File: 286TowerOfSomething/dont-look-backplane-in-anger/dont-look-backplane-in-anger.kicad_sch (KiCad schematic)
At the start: 1 part, among them J1 Bus_ISA_16bit

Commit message: More work on dont-look-backplane-in-anger
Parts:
- added J2, J3, J4, J5, J6, J7: Bus_ISA_16bit, pc-parts:645169-3, symbol Connector:Bus_ISA_16bit
- J1: footprint (none) -> pc-parts:645169-3
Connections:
- net GND: now reaches J1.1 (GND)
- net GND: now also J1.10 (GND), J1.31 (GND), J1.80 (GND), J2.1 (GND), J2.10 (GND), J2.31 (GND), J2.80 (GND), J3.1 (GND), J3.10 (GND), J3.31 (GND), J3.80 (GND), J4.1 (GND), J4.10 (GND), J4.31 (GND), J4.80 (GND), J5.1 (GND), J5.10 (GND), J5.31 (GND), J5.80 (GND), J6.1 (GND), J6.10 (GND), J6.31 (GND), J6.80 (GND), J7.1 (GND), J7.10 (GND), J7.31 (GND), J7.80 (GND)
- net ~{MEMWR}: now reaches J1.11 (~{SMEMW})
- net ~{MEMWR}: now also J2.11 (~{SMEMW}), J3.11 (~{SMEMW}), J4.11 (~{SMEMW}), J5.11 (~{SMEMW}), J6.11 (~{SMEMW}), J7.11 (~{SMEMW})
- net ~{MEMRD}: now reaches J1.12 (~{SMEMR})
- net ~{MEMRD}: now also J2.12 (~{SMEMR}), J3.12 (~{SMEMR}), J4.12 (~{SMEMR}), J5.12 (~{SMEMR}), J6.12 (~{SMEMR}), J7.12 (~{SMEMR})
- net ~{IOW}: now reaches J1.13 (~{IOW})
- net ~{IOW}: now also J2.13 (~{IOW}), J3.13 (~{IOW}), J4.13 (~{IOW}), J5.13 (~{IOW}), J6.13 (~{IOW}), J7.13 (~{IOW})
- net ~{IOR}: now reaches J1.14 (~{IOR})
- net ~{IOR}: now also J2.14 (~{IOR}), J3.14 (~{IOR}), J4.14 (~{IOR}), J5.14 (~{IOR}), J6.14 (~{IOR}), J7.14 (~{IOR})
- net ~{DACK3}: now reaches J1.15 (~{DACK3})
- net ~{DACK3}: now also J2.15 (~{DACK3}), J3.15 (~{DACK3}), J4.15 (~{DACK3}), J5.15 (~{DACK3}), J6.15 (~{DACK3}), J7.15 (~{DACK3})
- net DRQ3: now reaches J1.16 (DRQ3)
- net DRQ3: now also J2.16 (DRQ3), J3.16 (DRQ3), J4.16 (DRQ3), J5.16 (DRQ3), J6.16 (DRQ3), J7.16 (DRQ3)
- net ~{DACK1}: now reaches J1.17 (~{DACK1})
- net ~{DACK1}: now also J2.17 (~{DACK1}), J3.17 (~{DACK1}), J4.17 (~{DACK1}), J5.17 (~{DACK1}), J6.17 (~{DACK1}), J7.17 (~{DACK1})
- net DRQ1: now reaches J1.18 (DRQ1)
- net DRQ1: now also J2.18 (DRQ1), J3.18 (DRQ1), J4.18 (DRQ1), J5.18 (DRQ1), J6.18 (DRQ1), J7.18 (DRQ1)
- net ~{REFRESH}: now reaches J1.19 (~{REFRESH})
- net ~{REFRESH}: now also J2.19 (~{REFRESH}), J3.19 (~{REFRESH}), J4.19 (~{REFRESH}), J5.19 (~{REFRESH}), J6.19 (~{REFRESH}), J7.19 (~{REFRESH})
- net RESET: now reaches J1.2 (RESET)
- net RESET: now also J2.2 (RESET), J3.2 (RESET), J4.2 (RESET), J5.2 (RESET), J6.2 (RESET), J7.2 (RESET)
- net CLK: now reaches J1.20 (CLK)
- net CLK: now also J2.20 (CLK), J3.20 (CLK), J4.20 (CLK), J5.20 (CLK), J6.20 (CLK), J7.20 (CLK)
- net IRQ7: now reaches J1.21 (IRQ7)
- net IRQ7: now also J2.21 (IRQ7), J3.21 (IRQ7), J4.21 (IRQ7), J5.21 (IRQ7), J6.21 (IRQ7), J7.21 (IRQ7)
- net IRQ6: now reaches J1.22 (IRQ6)
- net IRQ6: now also J2.22 (IRQ6), J3.22 (IRQ6), J4.22 (IRQ6), J5.22 (IRQ6), J6.22 (IRQ6), J7.22 (IRQ6)
- net IRQ5: now reaches J1.23 (IRQ5)
- net IRQ5: now also J2.23 (IRQ5), J3.23 (IRQ5), J4.23 (IRQ5), J5.23 (IRQ5), J6.23 (IRQ5), J7.23 (IRQ5)
- net IRQ4: now reaches J1.24 (IRQ4)
- net IRQ4: now also J2.24 (IRQ4), J3.24 (IRQ4), J4.24 (IRQ4), J5.24 (IRQ4), J6.24 (IRQ4), J7.24 (IRQ4)
- net IRQ3: now reaches J1.25 (IRQ3)
- net IRQ3: now also J2.25 (IRQ3), J3.25 (IRQ3), J4.25 (IRQ3), J5.25 (IRQ3), J6.25 (IRQ3), J7.25 (IRQ3)
- net ~{DACK2}: now reaches J1.26 (~{DACK2})
- net ~{DACK2}: now also J2.26 (~{DACK2}), J3.26 (~{DACK2}), J4.26 (~{DACK2}), J5.26 (~{DACK2}), J6.26 (~{DACK2}), J7.26 (~{DACK2})
- net TC: now reaches J1.27 (TC)
- net TC: now also J2.27 (TC), J3.27 (TC), J4.27 (TC), J5.27 (TC), J6.27 (TC), J7.27 (TC)
- net ALE: now reaches J1.28 (ALE)
- net ALE: now also J2.28 (ALE), J3.28 (ALE), J4.28 (ALE), J5.28 (ALE), J6.28 (ALE), J7.28 (ALE)
- net +5V: now reaches J1.29 (VCC)
- net +5V: now also J1.3 (+5V), J1.78 (+5V), J2.29 (VCC), J2.3 (+5V), J2.78 (+5V), J3.29 (VCC), J3.3 (+5V), J3.78 (+5V), J4.29 (VCC), J4.3 (+5V), J4.78 (+5V), J5.29 (VCC), J5.3 (+5V), J5.78 (+5V), J6.29 (VCC), J6.3 (+5V), J6.78 (+5V), J7.29 (VCC), J7.3 (+5V), J7.78 (+5V)
- net OSC: now reaches J1.30 (OSC)
- net OSC: now also J2.30 (OSC), J3.30 (OSC), J4.30 (OSC), J5.30 (OSC), J6.30 (OSC), J7.30 (OSC)
- net IO: now reaches J1.32 (IO)
- net IO: now also J2.32 (IO), J3.32 (IO), J4.32 (IO), J5.32 (IO), J6.32 (IO), J7.32 (IO)
- net D7: now reaches J1.33 (DB7)
- net D7: now also J2.33 (DB7), J3.33 (DB7), J4.33 (DB7), J5.33 (DB7), J6.33 (DB7), J7.33 (DB7)
- net D6: now reaches J1.34 (DB6)
- net D6: now also J2.34 (DB6), J3.34 (DB6), J4.34 (DB6), J5.34 (DB6), J6.34 (DB6), J7.34 (DB6)
- net D5: now reaches J1.35 (DB5)
- net D5: now also J2.35 (DB5), J3.35 (DB5), J4.35 (DB5), J5.35 (DB5), J6.35 (DB5), J7.35 (DB5)
- net D4: now reaches J1.36 (DB4)
- net D4: now also J2.36 (DB4), J3.36 (DB4), J4.36 (DB4), J5.36 (DB4), J6.36 (DB4), J7.36 (DB4)
- net D3: now reaches J1.37 (DB3)
- net D3: now also J2.37 (DB3), J3.37 (DB3), J4.37 (DB3), J5.37 (DB3), J6.37 (DB3), J7.37 (DB3)
- net D2: now reaches J1.38 (DB2)
- net D2: now also J2.38 (DB2), J3.38 (DB2), J4.38 (DB2), J5.38 (DB2), J6.38 (DB2), J7.38 (DB2)
- net D1: now reaches J1.39 (DB1)
- net D1: now also J2.39 (DB1), J3.39 (DB1), J4.39 (DB1), J5.39 (DB1), J6.39 (DB1), J7.39 (DB1)
- net IRQ2: now reaches J1.4 (IRQ2)
- net IRQ2: now also J2.4 (IRQ2), J3.4 (IRQ2), J4.4 (IRQ2), J5.4 (IRQ2), J6.4 (IRQ2), J7.4 (IRQ2)
- net D0: now reaches J1.40 (DB0)
- net D0: now also J2.40 (DB0), J3.40 (DB0), J4.40 (DB0), J5.40 (DB0), J6.40 (DB0), J7.40 (DB0)
- net IORDY: now reaches J1.41 (IO_READY)
- net IORDY: now also J2.41 (IO_READY), J3.41 (IO_READY), J4.41 (IO_READY), J5.41 (IO_READY), J6.41 (IO_READY), J7.41 (IO_READY)
- net AEN: now reaches J1.42 (AEN)
- net AEN: now also J2.42 (AEN), J3.42 (AEN), J4.42 (AEN), J5.42 (AEN), J6.42 (AEN), J7.42 (AEN)
- net A19: now reaches J1.43 (BA19)
- net A19: now also J2.43 (BA19), J3.43 (BA19), J4.43 (BA19), J5.43 (BA19), J6.43 (BA19), J7.43 (BA19)
- net A18: now reaches J1.44 (BA18)
- net A18: now also J2.44 (BA18), J3.44 (BA18), J4.44 (BA18), J5.44 (BA18), J6.44 (BA18), J7.44 (BA18)
- net A17: now reaches J1.45 (BA17)
- net A17: now also J2.45 (BA17), J3.45 (BA17), J4.45 (BA17), J5.45 (BA17), J6.45 (BA17), J7.45 (BA17)
- net A16: now reaches J1.46 (BA16)
- net A16: now also J2.46 (BA16), J3.46 (BA16), J4.46 (BA16), J5.46 (BA16), J6.46 (BA16), J7.46 (BA16)
- net A15: now reaches J1.47 (BA15)
- net A15: now also J2.47 (BA15), J3.47 (BA15), J4.47 (BA15), J5.47 (BA15), J6.47 (BA15), J7.47 (BA15)
- net A14: now reaches J1.48 (BA14)
- net A14: now also J2.48 (BA14), J3.48 (BA14), J4.48 (BA14), J5.48 (BA14), J6.48 (BA14), J7.48 (BA14)
- net A13: now reaches J1.49 (BA13)
- net A13: now also J2.49 (BA13), J3.49 (BA13), J4.49 (BA13), J5.49 (BA13), J6.49 (BA13), J7.49 (BA13)
- net -5V: now reaches J1.5 (-5V)
- net -5V: now also J2.5 (-5V), J3.5 (-5V), J4.5 (-5V), J5.5 (-5V), J6.5 (-5V), J7.5 (-5V)
- net A12: now reaches J1.50 (BA12)
- net A12: now also J2.50 (BA12), J3.50 (BA12), J4.50 (BA12), J5.50 (BA12), J6.50 (BA12), J7.50 (BA12)
- net A11: now reaches J1.51 (BA11)
- net A11: now also J2.51 (BA11), J3.51 (BA11), J4.51 (BA11), J5.51 (BA11), J6.51 (BA11), J7.51 (BA11)
- net A10: now reaches J1.52 (BA10)
- net A10: now also J2.52 (BA10), J3.52 (BA10), J4.52 (BA10), J5.52 (BA10), J6.52 (BA10), J7.52 (BA10)
- net A9: now reaches J1.53 (BA09)
- net A9: now also J2.53 (BA09), J3.53 (BA09), J4.53 (BA09), J5.53 (BA09), J6.53 (BA09), J7.53 (BA09)
- net A8: now reaches J1.54 (BA08)
- net A8: now also J2.54 (BA08), J3.54 (BA08), J4.54 (BA08), J5.54 (BA08), J6.54 (BA08), J7.54 (BA08)
- net A7: now reaches J1.55 (BA07)
- net A7: now also J2.55 (BA07), J3.55 (BA07), J4.55 (BA07), J5.55 (BA07), J6.55 (BA07), J7.55 (BA07)
- net A6: now reaches J1.56 (BA06)
- net A6: now also J2.56 (BA06), J3.56 (BA06), J4.56 (BA06), J5.56 (BA06), J6.56 (BA06), J7.56 (BA06)
- net A5: now reaches J1.57 (BA05)
- net A5: now also J2.57 (BA05), J3.57 (BA05), J4.57 (BA05), J5.57 (BA05), J6.57 (BA05), J7.57 (BA05)
- net A4: now reaches J1.58 (BA04)
- net A4: now also J2.58 (BA04), J3.58 (BA04), J4.58 (BA04), J5.58 (BA04), J6.58 (BA04), J7.58 (BA04)
- net A3: now reaches J1.59 (BA03)
- net A3: now also J2.59 (BA03), J3.59 (BA03), J4.59 (BA03), J5.59 (BA03), J6.59 (BA03), J7.59 (BA03)
- net DRQ2: now reaches J1.6 (DRQ2)
- net DRQ2: now also J2.6 (DRQ2), J3.6 (DRQ2), J4.6 (DRQ2), J5.6 (DRQ2), J6.6 (DRQ2), J7.6 (DRQ2)
- net A2: now reaches J1.60 (BA02)
- net A2: now also J2.60 (BA02), J3.60 (BA02), J4.60 (BA02), J5.60 (BA02), J6.60 (BA02), J7.60 (BA02)
- net A1: now reaches J1.61 (BA01)
- net A1: now also J2.61 (BA01), J3.61 (BA01), J4.61 (BA01), J5.61 (BA01), J6.61 (BA01), J7.61 (BA01)
- net A0: now reaches J1.62 (BA00)
- net A0: now also J2.62 (BA00), J3.62 (BA00), J4.62 (BA00), J5.62 (BA00), J6.62 (BA00), J7.62 (BA00)
- net ~{MEMCS16}: now reaches J1.63 (~{MEMCS16})
- net ~{MEMCS16}: now also J2.63 (~{MEMCS16}), J3.63 (~{MEMCS16}), J4.63 (~{MEMCS16}), J5.63 (~{MEMCS16}), J6.63 (~{MEMCS16}), J7.63 (~{MEMCS16})
- net ~{IOCS16}: now reaches J1.64 (~{IOCS16})
- net ~{IOCS16}: now also J2.64 (~{IOCS16}), J3.64 (~{IOCS16}), J4.64 (~{IOCS16}), J5.64 (~{IOCS16}), J6.64 (~{IOCS16}), J7.64 (~{IOCS16})
- net IRQ10: now reaches J1.65 (IRQ10)
- net IRQ10: now also J2.65 (IRQ10), J3.65 (IRQ10), J4.65 (IRQ10), J5.65 (IRQ10), J6.65 (IRQ10), J7.65 (IRQ10)
- net IRQ11: now reaches J1.66 (IRQ11)
- net IRQ11: now also J2.66 (IRQ11), J3.66 (IRQ11), J4.66 (IRQ11), J5.66 (IRQ11), J6.66 (IRQ11), J7.66 (IRQ11)
- net IRQ12: now reaches J1.67 (IRQ12)
- net IRQ12: now also J2.67 (IRQ12), J3.67 (IRQ12), J4.67 (IRQ12), J5.67 (IRQ12), J6.67 (IRQ12), J7.67 (IRQ12)
- net IRQ15: now reaches J1.68 (IRQ15)
- net IRQ15: now also J2.68 (IRQ15), J3.68 (IRQ15), J4.68 (IRQ15), J5.68 (IRQ15), J6.68 (IRQ15), J7.68 (IRQ15)
- net IRQ14: now reaches J1.69 (IRQ14)
- net IRQ14: now also J2.69 (IRQ14), J3.69 (IRQ14), J4.69 (IRQ14), J5.69 (IRQ14), J6.69 (IRQ14), J7.69 (IRQ14)
- net -12V: now reaches J1.7 (-12V)
- net -12V: now also J2.7 (-12V), J3.7 (-12V), J4.7 (-12V), J5.7 (-12V), J6.7 (-12V), J7.7 (-12V)
- net ~{DACK0}: now reaches J1.70 (~{DACK0})
- net ~{DACK0}: now also J2.70 (~{DACK0}), J3.70 (~{DACK0}), J4.70 (~{DACK0}), J5.70 (~{DACK0}), J6.70 (~{DACK0}), J7.70 (~{DACK0})
- net DRQ0: now reaches J1.71 (DRQ0)
- net DRQ0: now also J2.71 (DRQ0), J3.71 (DRQ0), J4.71 (DRQ0), J5.71 (DRQ0), J6.71 (DRQ0), J7.71 (DRQ0)
- net ~{DACK5}: now reaches J1.72 (~{DACK5})
- net ~{DACK5}: now also J2.72 (~{DACK5}), J3.72 (~{DACK5}), J4.72 (~{DACK5}), J5.72 (~{DACK5}), J6.72 (~{DACK5}), J7.72 (~{DACK5})
- net DRQ5: now reaches J1.73 (DRQ5)
- net DRQ5: now also J2.73 (DRQ5), J3.73 (DRQ5), J4.73 (DRQ5), J5.73 (DRQ5), J6.73 (DRQ5), J7.73 (DRQ5)
- net ~{DACK6}: now reaches J1.74 (~{DACK6})
- net ~{DACK6}: now also J2.74 (~{DACK6}), J3.74 (~{DACK6}), J4.74 (~{DACK6}), J5.74 (~{DACK6}), J6.74 (~{DACK6}), J7.74 (~{DACK6})
- net DRQ6: now reaches J1.75 (DRQ6)
- net DRQ6: now also J2.75 (DRQ6), J3.75 (DRQ6), J4.75 (DRQ6), J5.75 (DRQ6), J6.75 (DRQ6), J7.75 (DRQ6)
- net ~{DACK7}: now reaches J1.76 (~{DACK7})
- net ~{DACK7}: now also J2.76 (~{DACK7}), J3.76 (~{DACK7}), J4.76 (~{DACK7}), J5.76 (~{DACK7}), J6.76 (~{DACK7}), J7.76 (~{DACK7})
- net DRQ7: now reaches J1.77 (DRQ7)
- net DRQ7: now also J2.77 (DRQ7), J3.77 (DRQ7), J4.77 (DRQ7), J5.77 (DRQ7), J6.77 (DRQ7), J7.77 (DRQ7)
- net MASTER: now reaches J1.79 (MASTER)
- net MASTER: now also J2.79 (MASTER), J3.79 (MASTER), J4.79 (MASTER), J5.79 (MASTER), J6.79 (MASTER), J7.79 (MASTER)
- net SBHE: now reaches J1.81 (SBHE)
- net SBHE: now also J2.81 (SBHE), J3.81 (SBHE), J4.81 (SBHE), J5.81 (SBHE), J6.81 (SBHE), J7.81 (SBHE)
- net LA23: now reaches J1.82 (LA23)
- net LA23: now also J2.82 (LA23), J3.82 (LA23), J4.82 (LA23), J5.82 (LA23), J6.82 (LA23), J7.82 (LA23)
- net LA22: now reaches J1.83 (LA22)
- net LA22: now also J2.83 (LA22), J3.83 (LA22), J4.83 (LA22), J5.83 (LA22), J6.83 (LA22), J7.83 (LA22)
- net LA21: now reaches J1.84 (LA21)
- net LA21: now also J2.84 (LA21), J3.84 (LA21), J4.84 (LA21), J5.84 (LA21), J6.84 (LA21), J7.84 (LA21)
- net LA20: now reaches J1.85 (LA20)
- net LA20: now also J2.85 (LA20), J3.85 (LA20), J4.85 (LA20), J5.85 (LA20), J6.85 (LA20), J7.85 (LA20)
- net LA19: now reaches J1.86 (LA19)
- net LA19: now also J2.86 (LA19), J3.86 (LA19), J4.86 (LA19), J5.86 (LA19), J6.86 (LA19), J7.86 (LA19)
- net LA18: now reaches J1.87 (LA18)
- net LA18: now also J2.87 (LA18), J3.87 (LA18), J4.87 (LA18), J5.87 (LA18), J6.87 (LA18), J7.87 (LA18)
- net LA17: now reaches J1.88 (LA17)
- net LA17: now also J2.88 (LA17), J3.88 (LA17), J4.88 (LA17), J5.88 (LA17), J6.88 (LA17), J7.88 (LA17)
- net ~{MEMR}: now reaches J1.89 (~{MEMR})
- net ~{MEMR}: now also J2.89 (~{MEMR}), J3.89 (~{MEMR}), J4.89 (~{MEMR}), J5.89 (~{MEMR}), J6.89 (~{MEMR}), J7.89 (~{MEMR})
- net +12V: now reaches J1.9 (+12V)
- net +12V: now also J2.9 (+12V), J3.9 (+12V), J4.9 (+12V), J5.9 (+12V), J6.9 (+12V), J7.9 (+12V)
- net ~{MEMW}: now reaches J1.90 (~{MEMW})
- net ~{MEMW}: now also J2.90 (~{MEMW}), J3.90 (~{MEMW}), J4.90 (~{MEMW}), J5.90 (~{MEMW}), J6.90 (~{MEMW}), J7.90 (~{MEMW})
- net D8: now reaches J1.91 (D8)
- net D8: now also J2.91 (D8), J3.91 (D8), J4.91 (D8), J5.91 (D8), J6.91 (D8), J7.91 (D8)
- net D9: now reaches J1.92 (D9)
- net D9: now also J2.92 (D9), J3.92 (D9), J4.92 (D9), J5.92 (D9), J6.92 (D9), J7.92 (D9)
- net D10: now reaches J1.93 (D10)
- net D10: now also J2.93 (D10), J3.93 (D10), J4.93 (D10), J5.93 (D10), J6.93 (D10), J7.93 (D10)
- net D11: now reaches J1.94 (D11)
- net D11: now also J2.94 (D11), J3.94 (D11), J4.94 (D11), J5.94 (D11), J6.94 (D11), J7.94 (D11)
- net D12: now reaches J1.95 (D12)
- net D12: now also J2.95 (D12), J3.95 (D12), J4.95 (D12), J5.95 (D12), J6.95 (D12), J7.95 (D12)
- net D13: now reaches J1.96 (D13)
- net D13: now also J2.96 (D13), J3.96 (D13), J4.96 (D13), J5.96 (D13), J6.96 (D13), J7.96 (D13)
- net D14: now reaches J1.97 (D14)
- net D14: now also J2.97 (D14), J3.97 (D14), J4.97 (D14), J5.97 (D14), J6.97 (D14), J7.97 (D14)
- net D15: now reaches J1.98 (D15)
- net D15: now also J2.98 (D15), J3.98 (D15), J4.98 (D15), J5.98 (D15), J6.98 (D15), J7.98 (D15)
- no-connect marks 0 -> 7

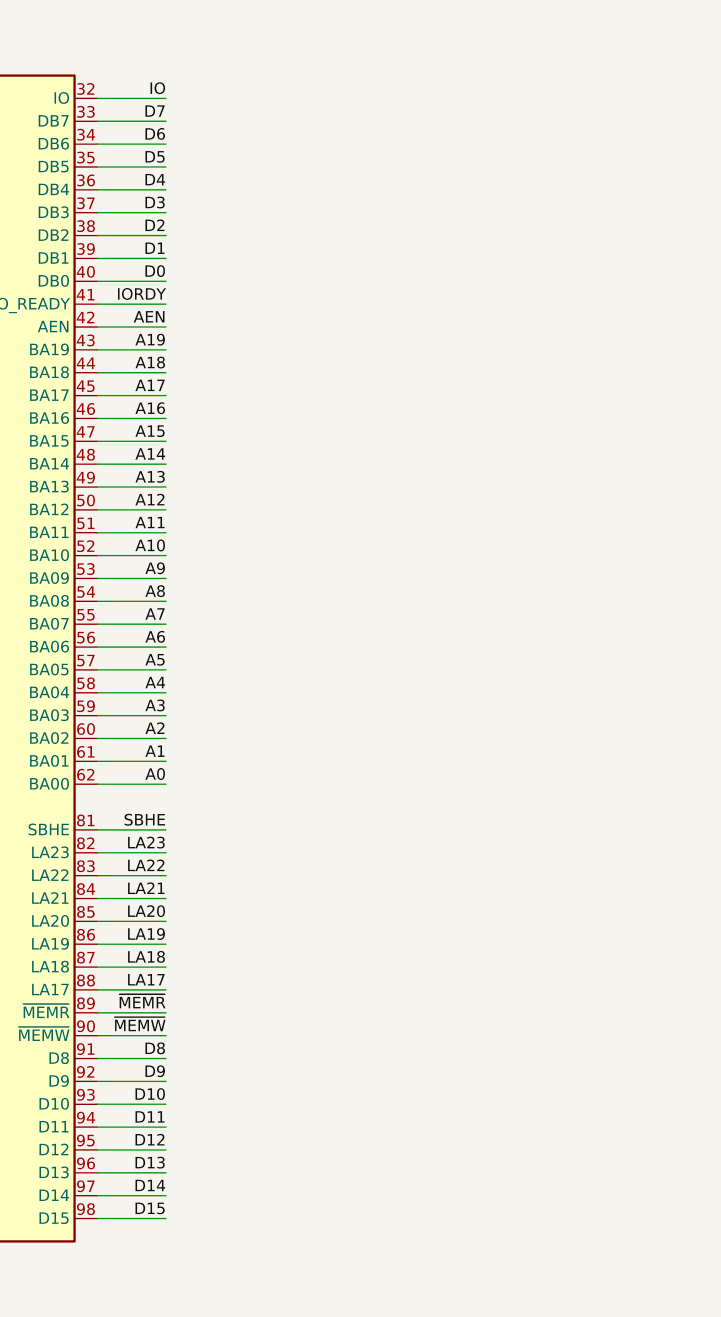
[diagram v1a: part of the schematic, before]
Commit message: Adding an eighth slot to the backplane
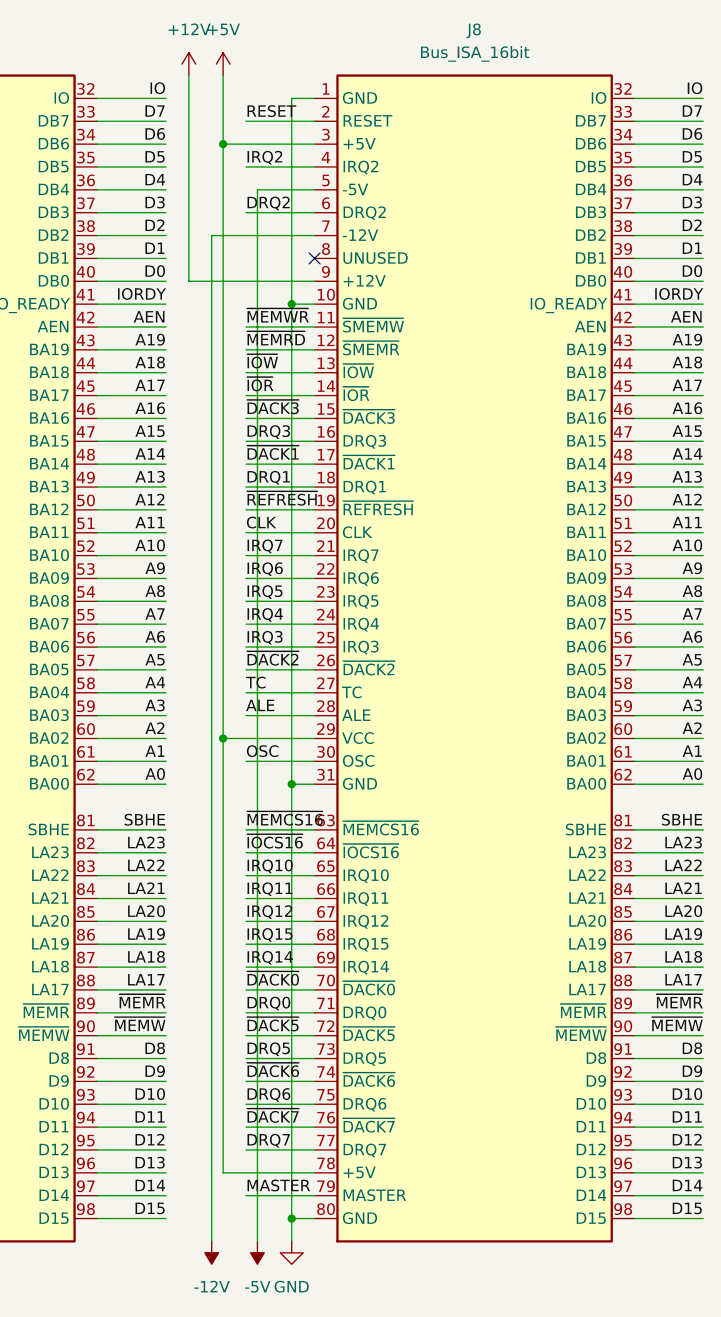
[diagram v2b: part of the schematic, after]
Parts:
- added J8: Bus_ISA_16bit, pc-parts:645169-3, symbol Connector:Bus_ISA_16bit
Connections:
- net +12V: now also J8.9 (+12V)
- net +5V: now also J8.29 (VCC), J8.3 (+5V), J8.78 (+5V)
- net -12V: now also J8.7 (-12V)
- net -5V: now also J8.5 (-5V)
- net A0: now also J8.62 (BA00)
- net A1: now also J8.61 (BA01)
- net A10: now also J8.52 (BA10)
- net A11: now also J8.51 (BA11)
- net A12: now also J8.50 (BA12)
- net A13: now also J8.49 (BA13)
- net A14: now also J8.48 (BA14)
- net A15: now also J8.47 (BA15)
- net A16: now also J8.46 (BA16)
- net A17: now also J8.45 (BA17)
- net A18: now also J8.44 (BA18)
- net A19: now also J8.43 (BA19)
- net A2: now also J8.60 (BA02)
- net A3: now also J8.59 (BA03)
- net A4: now also J8.58 (BA04)
- net A5: now also J8.57 (BA05)
- net A6: now also J8.56 (BA06)
- net A7: now also J8.55 (BA07)
- net A8: now also J8.54 (BA08)
- net A9: now also J8.53 (BA09)
- net AEN: now also J8.42 (AEN)
- net ALE: now also J8.28 (ALE)
- net CLK: now also J8.20 (CLK)
- net D0: now also J8.40 (DB0)
- net D1: now also J8.39 (DB1)
- net D10: now also J8.93 (D10)
- net D11: now also J8.94 (D11)
- net D12: now also J8.95 (D12)
- net D13: now also J8.96 (D13)
- net D14: now also J8.97 (D14)
- net D15: now also J8.98 (D15)
- net D2: now also J8.38 (DB2)
- net D3: now also J8.37 (DB3)
- net D4: now also J8.36 (DB4)
- net D5: now also J8.35 (DB5)
- net D6: now also J8.34 (DB6)
- net D7: now also J8.33 (DB7)
- net D8: now also J8.91 (D8)
- net D9: now also J8.92 (D9)
- net DRQ0: now also J8.71 (DRQ0)
- net DRQ1: now also J8.18 (DRQ1)
- net DRQ2: now also J8.6 (DRQ2)
- net DRQ3: now also J8.16 (DRQ3)
- net DRQ5: now also J8.73 (DRQ5)
- net DRQ6: now also J8.75 (DRQ6)
- net DRQ7: now also J8.77 (DRQ7)
- net GND: now also J8.1 (GND), J8.10 (GND), J8.31 (GND), J8.80 (GND)
- net IO: now also J8.32 (IO)
- net IORDY: now also J8.41 (IO_READY)
- net IRQ10: now also J8.65 (IRQ10)
- net IRQ11: now also J8.66 (IRQ11)
- net IRQ12: now also J8.67 (IRQ12)
- net IRQ14: now also J8.69 (IRQ14)
- net IRQ15: now also J8.68 (IRQ15)
- net IRQ2: now also J8.4 (IRQ2)
- net IRQ3: now also J8.25 (IRQ3)
- net IRQ4: now also J8.24 (IRQ4)
- net IRQ5: now also J8.23 (IRQ5)
- net IRQ6: now also J8.22 (IRQ6)
- net IRQ7: now also J8.21 (IRQ7)
- net LA17: now also J8.88 (LA17)
- net LA18: now also J8.87 (LA18)
- net LA19: now also J8.86 (LA19)
- net LA20: now also J8.85 (LA20)
- net LA21: now also J8.84 (LA21)
- net LA22: now also J8.83 (LA22)
- net LA23: now also J8.82 (LA23)
- net MASTER: now also J8.79 (MASTER)
- net OSC: now also J8.30 (OSC)
- net RESET: now also J8.2 (RESET)
- net SBHE: now also J8.81 (SBHE)
- net TC: now also J8.27 (TC)
- net ~{DACK0}: now also J8.70 (~{DACK0})
- net ~{DACK1}: now also J8.17 (~{DACK1})
- net ~{DACK2}: now also J8.26 (~{DACK2})
- net ~{DACK3}: now also J8.15 (~{DACK3})
- net ~{DACK5}: now also J8.72 (~{DACK5})
- net ~{DACK6}: now also J8.74 (~{DACK6})
- net ~{DACK7}: now also J8.76 (~{DACK7})
- net ~{IOCS16}: now also J8.64 (~{IOCS16})
- net ~{IOR}: now also J8.14 (~{IOR})
- net ~{IOW}: now also J8.13 (~{IOW})
- net ~{MEMCS16}: now also J8.63 (~{MEMCS16})
- net ~{MEMRD}: now also J8.12 (~{SMEMR})
- net ~{MEMR}: now also J8.89 (~{MEMR})
- net ~{MEMWR}: now also J8.11 (~{SMEMW})
- net ~{MEMW}: now also J8.90 (~{MEMW})
- net ~{REFRESH}: now also J8.19 (~{REFRESH})
- no-connect marks 7 -> 8
